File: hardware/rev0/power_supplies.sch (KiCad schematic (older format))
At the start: 35 parts, among them IC1 ECP5-BGA256, U3 MIC5219-3.3YM5, U4 TCR2EE11, U5 MIC5504-2.5YM5

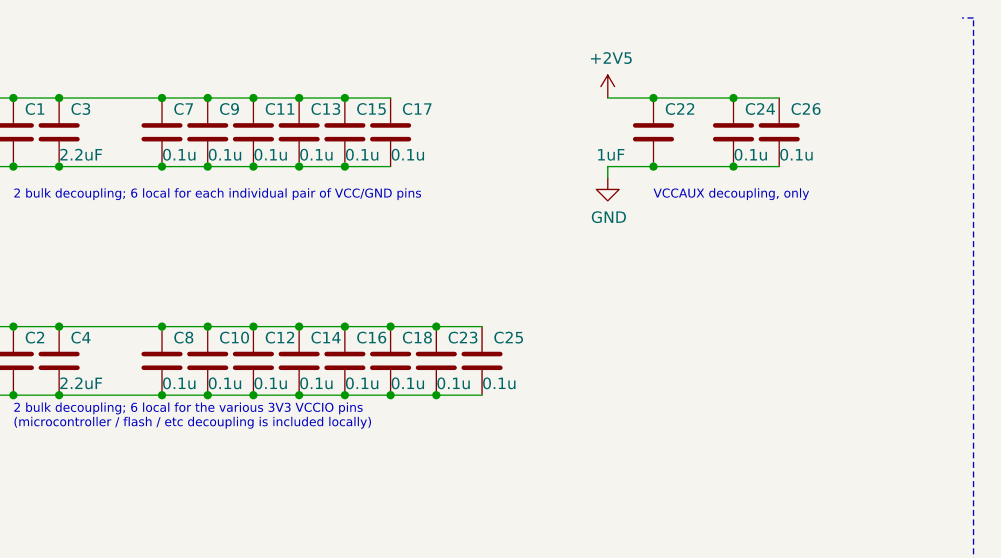
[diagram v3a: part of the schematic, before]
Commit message: Tidy up component values
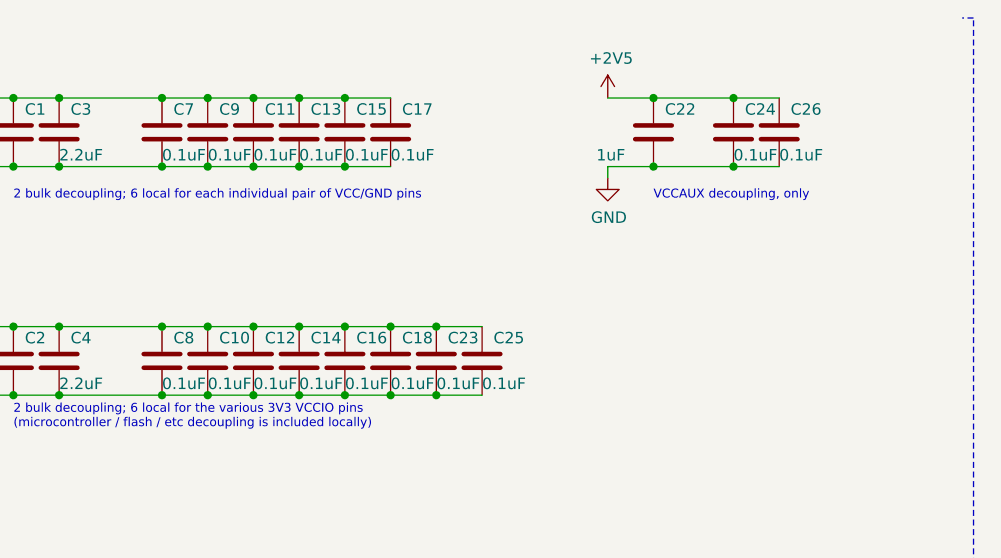
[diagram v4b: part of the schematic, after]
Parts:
- C10, C11, C12, C13, C14, C15, C16, C17, C18, C23, C24, C25, C26, C7, C8, C9: value 0.1u -> 0.1uF
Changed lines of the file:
@@
 P 1700 1000
 F 0 "C7" H 1750 1100 50  0000 L CNN
-F 1 "0.1u" H 1700 900 50  0000 L CNN
+F 1 "0.1uF" H 1700 900 50  0000 L CNN
 F 2 "Capacitor_SMD:C_0402_1005Metric" H 1738 850 50  0001 C CNN
 F 3 "~" H 1700 1000 50  0001 C CNN
@@
 P 1900 1000
 F 0 "C9" H 1950 1100 50  0000 L CNN
-F 1 "0.1u" H 1900 900 50  0000 L CNN
+F 1 "0.1uF" H 1900 900 50  0000 L CNN
 F 2 "Capacitor_SMD:C_0402_1005Metric" H 1938 850 50  0001 C CNN
 F 3 "~" H 1900 1000 50  0001 C CNN
@@
 P 2100 1000
 F 0 "C11" H 2150 1100 50  0000 L CNN
-F 1 "0.1u" H 2100 900 50  0000 L CNN
+F 1 "0.1uF" H 2100 900 50  0000 L CNN
 F 2 "Capacitor_SMD:C_0402_1005Metric" H 2138 850 50  0001 C CNN
 F 3 "~" H 2100 1000 50  0001 C CNN
@@
 P 2300 1000
 F 0 "C13" H 2350 1100 50  0000 L CNN
-F 1 "0.1u" H 2300 900 50  0000 L CNN
+F 1 "0.1uF" H 2300 900 50  0000 L CNN
 F 2 "Capacitor_SMD:C_0402_1005Metric" H 2338 850 50  0001 C CNN
 F 3 "~" H 2300 1000 50  0001 C CNN
@@
 P 2500 1000
 F 0 "C15" H 2550 1100 50  0000 L CNN
-F 1 "0.1u" H 2500 900 50  0000 L CNN
+F 1 "0.1uF" H 2500 900 50  0000 L CNN
 F 2 "Capacitor_SMD:C_0402_1005Metric" H 2538 850 50  0001 C CNN
 F 3 "~" H 2500 1000 50  0001 C CNN
@@
 P 2700 1000
 F 0 "C17" H 2750 1100 50  0000 L CNN
-F 1 "0.1u" H 2700 900 50  0000 L CNN
+F 1 "0.1uF" H 2700 900 50  0000 L CNN
 F 2 "Capacitor_SMD:C_0402_1005Metric" H 2738 850 50  0001 C CNN
 F 3 "~" H 2700 1000 50  0001 C CNN
@@
 P 2500 2000
 F 0 "C16" H 2550 2100 50  0000 L CNN
-F 1 "0.1u" H 2500 1900 50  0000 L CNN
+F 1 "0.1uF" H 2500 1900 50  0000 L CNN
 F 2 "Capacitor_SMD:C_0402_1005Metric" H 2538 1850 50  0001 C CNN
 F 3 "~" H 2500 2000 50  0001 C CNN
@@
 P 2300 2000
 F 0 "C14" H 2350 2100 50  0000 L CNN
-F 1 "0.1u" H 2300 1900 50  0000 L CNN
+F 1 "0.1uF" H 2300 1900 50  0000 L CNN
 F 2 "Capacitor_SMD:C_0402_1005Metric" H 2338 1850 50  0001 C CNN
 F 3 "~" H 2300 2000 50  0001 C CNN
@@
 P 2100 2000
 F 0 "C12" H 2150 2100 50  0000 L CNN
-F 1 "0.1u" H 2100 1900 50  0000 L CNN
+F 1 "0.1uF" H 2100 1900 50  0000 L CNN
 F 2 "Capacitor_SMD:C_0402_1005Metric" H 2138 1850 50  0001 C CNN
 F 3 "~" H 2100 2000 50  0001 C CNN
@@
 P 1900 2000
 F 0 "C10" H 1950 2100 50  0000 L CNN
-F 1 "0.1u" H 1900 1900 50  0000 L CNN
+F 1 "0.1uF" H 1900 1900 50  0000 L CNN
 F 2 "Capacitor_SMD:C_0402_1005Metric" H 1938 1850 50  0001 C CNN
 F 3 "~" H 1900 2000 50  0001 C CNN
@@
 P 1700 2000
 F 0 "C8" H 1750 2100 50  0000 L CNN
-F 1 "0.1u" H 1700 1900 50  0000 L CNN
+F 1 "0.1uF" H 1700 1900 50  0000 L CNN
 F 2 "Capacitor_SMD:C_0402_1005Metric" H 1738 1850 50  0001 C CNN
 F 3 "~" H 1700 2000 50  0001 C CNN
@@
 P 4200 1000
 F 0 "C24" H 4250 1100 50  0000 L CNN
-F 1 "0.1u" H 4200 900 50  0000 L CNN
+F 1 "0.1uF" H 4200 900 50  0000 L CNN
 F 2 "Capacitor_SMD:C_0402_1005Metric" H 4238 850 50  0001 C CNN
 F 3 "~" H 4200 1000 50  0001 C CNN
@@
 P 4400 1000
 F 0 "C26" H 4450 1100 50  0000 L CNN
-F 1 "0.1u" H 4400 900 50  0000 L CNN
+F 1 "0.1uF" H 4400 900 50  0000 L CNN
 F 2 "Capacitor_SMD:C_0402_1005Metric" H 4438 850 50  0001 C CNN
 F 3 "~" H 4400 1000 50  0001 C CNN
@@
 P 3100 2000
 F 0 "C25" H 3150 2100 50  0000 L CNN
-F 1 "0.1u" H 3100 1900 50  0000 L CNN
+F 1 "0.1uF" H 3100 1900 50  0000 L CNN
 F 2 "Capacitor_SMD:C_0402_1005Metric" H 3138 1850 50  0001 C CNN
 F 3 "~" H 3100 2000 50  0001 C CNN
@@
 P 2900 2000
 F 0 "C23" H 2950 2100 50  0000 L CNN
-F 1 "0.1u" H 2900 1900 50  0000 L CNN
+F 1 "0.1uF" H 2900 1900 50  0000 L CNN
 F 2 "Capacitor_SMD:C_0402_1005Metric" H 2938 1850 50  0001 C CNN
 F 3 "~" H 2900 2000 50  0001 C CNN
@@
 P 2700 2000
 F 0 "C18" H 2750 2100 50  0000 L CNN
-F 1 "0.1u" H 2700 1900 50  0000 L CNN
+F 1 "0.1uF" H 2700 1900 50  0000 L CNN
 F 2 "Capacitor_SMD:C_0402_1005Metric" H 2738 1850 50  0001 C CNN
 F 3 "~" H 2700 2000 50  0001 C CNN

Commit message: Pick part numbers for BOM
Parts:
- C1, C2, C20, C3, C4, C6: Manufacturer_Part_Number (none) -> LMK107B7105KA-T
- C10, C11, C12, C13, C14, C15, C16, C17, C18, C23, C24, C25, C26, C27, C7, C8, C9: Manufacturer_Part_Number (none) -> LMF105B7104KVHF
- C22, C28, C29, C30: Manufacturer_Part_Number (none) -> LMK107B7225KA-T
- C52: Manufacturer_Part_Number (none) -> UMK105BJ471KV-F
- U3: Manufacturer_Part_Number (none) -> MIC5219-3.3YM5-TR
- U4: Manufacturer_Part_Number (none) -> TCR2EE11,LM
- U5: Manufacturer_Part_Number (none) -> MIC5219-2.5YM5-TR
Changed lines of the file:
@@
 F 2 "Capacitor_SMD:C_0603_1608Metric" H 4488 5900 50  0001 C CNN
 F 3 "~" H 4450 6050 50  0001 C CNN
+F 4 "LMK107B7225KA-T" H 4450 6050 50  0001 C CNN "Manufacturer_Part_Number"
 	1    4450 6050
 	0    1    1    0
@@
 F 2 "Capacitor_SMD:C_0603_1608Metric" H 5938 6250 50  0001 C CNN
 F 3 "~" H 5900 6400 50  0001 C CNN
+F 4 "LMK107B7225KA-T" H 5900 6400 50  0001 C CNN "Manufacturer_Part_Number"
 	1    5900 6400
 	1    0    0    -1
@@
 F 2 "Package_TO_SOT_SMD:SOT-23-5" H 5350 5950 50  0001 C CNN
 F 3 "http://ww1.microchip.com/downloads/en/DeviceDoc/MIC550X.pdf" H 5100 6600 50  0001 C CNN
+F 4 "MIC5219-2.5YM5-TR" H 5350 6350 50  0001 C CNN "Manufacturer_Part_Number"
 	1    5350 6350
 	1    0    0    -1
@@
 F 2 "Capacitor_SMD:C_0603_1608Metric" H 1488 3750 50  0001 C CNN
 F 3 "~" H 1450 3900 50  0001 C CNN
+F 4 "LMK107B7105KA-T" H 1450 3900 50  0001 C CNN "Manufacturer_Part_Number"
 	1    1450 3900
 	0    1    1    0
@@
 F 2 "Capacitor_SMD:C_0603_1608Metric" H 2988 4100 50  0001 C CNN
 F 3 "~" H 2950 4250 50  0001 C CNN
+F 4 "LMK107B7105KA-T" H 2950 4250 50  0001 C CNN "Manufacturer_Part_Number"
 	1    2950 4250
 	1    0    0    -1
@@
 F 2 "Capacitor_SMD:C_0402_1005Metric" H 4488 3700 50  0001 C CNN
 F 3 "~" H 4450 3850 50  0001 C CNN
+F 4 "LMF105B7104KVHF" H 4450 3850 50  0001 C CNN "Manufacturer_Part_Number"
 	1    4450 3850
 	0    1    1    0
@@
 F 2 "Capacitor_SMD:C_0603_1608Metric" H 5938 4050 50  0001 C CNN
 F 3 "~" H 5900 4200 50  0001 C CNN
+F 4 "LMK107B7225KA-T" H 5900 4200 50  0001 C CNN "Manufacturer_Part_Number"
 	1    5900 4200
 	1    0    0    -1
@@
 F 2 "Capacitor_SMD:C_0402_1005Metric" H 1738 850 50  0001 C CNN
 F 3 "~" H 1700 1000 50  0001 C CNN
+F 4 "LMF105B7104KVHF" H 1700 1000 50  0001 C CNN "Manufacturer_Part_Number"
 	1    1700 1000
 	1    0    0    -1
@@
 F 2 "Capacitor_SMD:C_0402_1005Metric" H 1938 850 50  0001 C CNN
 F 3 "~" H 1900 1000 50  0001 C CNN
+F 4 "LMF105B7104KVHF" H 1900 1000 50  0001 C CNN "Manufacturer_Part_Number"
 	1    1900 1000
 	1    0    0    -1
@@
 F 2 "Capacitor_SMD:C_0402_1005Metric" H 2138 850 50  0001 C CNN
 F 3 "~" H 2100 1000 50  0001 C CNN
+F 4 "LMF105B7104KVHF" H 2100 1000 50  0001 C CNN "Manufacturer_Part_Number"
 	1    2100 1000
 	1    0    0    -1
@@
 F 2 "Capacitor_SMD:C_0402_1005Metric" H 2338 850 50  0001 C CNN
 F 3 "~" H 2300 1000 50  0001 C CNN
+F 4 "LMF105B7104KVHF" H 2300 1000 50  0001 C CNN "Manufacturer_Part_Number"
 	1    2300 1000
 	1    0    0    -1
@@
 F 2 "Capacitor_SMD:C_0402_1005Metric" H 2538 850 50  0001 C CNN
 F 3 "~" H 2500 1000 50  0001 C CNN
+F 4 "LMF105B7104KVHF" H 2500 1000 50  0001 C CNN "Manufacturer_Part_Number"
 	1    2500 1000
 	1    0    0    -1
@@
 F 2 "Capacitor_SMD:C_0402_1005Metric" H 2738 850 50  0001 C CNN
 F 3 "~" H 2700 1000 50  0001 C CNN
+F 4 "LMF105B7104KVHF" H 2700 1000 50  0001 C CNN "Manufacturer_Part_Number"
 	1    2700 1000
 	1    0    0    -1
@@
 F 2 "Capacitor_SMD:C_0603_1608Metric" H 1088 850 50  0001 C CNN
 F 3 "~" H 1050 1000 50  0001 C CNN
+F 4 "LMK107B7105KA-T" H 1050 1000 50  0001 C CNN "Manufacturer_Part_Number"
 	1    1050 1000
 	1    0    0    -1
@@
 F 2 "Capacitor_SMD:C_0603_1608Metric" H 1288 850 50  0001 C CNN
 F 3 "~" H 1250 1000 50  0001 C CNN
+F 4 "LMK107B7105KA-T" H 1250 1000 50  0001 C CNN "Manufacturer_Part_Number"
 	1    1250 1000
 	1    0    0    -1
@@
 F 2 "Capacitor_SMD:C_0603_1608Metric" H 1288 1850 50  0001 C CNN
 F 3 "~" H 1250 2000 50  0001 C CNN
+F 4 "LMK107B7105KA-T" H 1250 2000 50  0001 C CNN "Manufacturer_Part_Number"
 	1    1250 2000
 	1    0    0    -1
@@
 F 2 "Capacitor_SMD:C_0603_1608Metric" H 1088 1850 50  0001 C CNN
 F 3 "~" H 1050 2000 50  0001 C CNN
+F 4 "LMK107B7105KA-T" H 1050 2000 50  0001 C CNN "Manufacturer_Part_Number"
 	1    1050 2000
 	1    0    0    -1
@@
 F 2 "Capacitor_SMD:C_0402_1005Metric" H 2538 1850 50  0001 C CNN
 F 3 "~" H 2500 2000 50  0001 C CNN
+F 4 "LMF105B7104KVHF" H 2500 2000 50  0001 C CNN "Manufacturer_Part_Number"
 	1    2500 2000
 	1    0    0    -1
@@
 F 2 "Capacitor_SMD:C_0402_1005Metric" H 2338 1850 50  0001 C CNN
 F 3 "~" H 2300 2000 50  0001 C CNN
+F 4 "LMF105B7104KVHF" H 2300 2000 50  0001 C CNN "Manufacturer_Part_Number"
 	1    2300 2000
 	1    0    0    -1
@@
 F 2 "Capacitor_SMD:C_0402_1005Metric" H 2138 1850 50  0001 C CNN
 F 3 "~" H 2100 2000 50  0001 C CNN
+F 4 "LMF105B7104KVHF" H 2100 2000 50  0001 C CNN "Manufacturer_Part_Number"
 	1    2100 2000
 	1    0    0    -1
@@
 F 2 "Capacitor_SMD:C_0402_1005Metric" H 1938 1850 50  0001 C CNN
 F 3 "~" H 1900 2000 50  0001 C CNN
+F 4 "LMF105B7104KVHF" H 1900 2000 50  0001 C CNN "Manufacturer_Part_Number"
 	1    1900 2000
 	1    0    0    -1
@@
 F 2 "Capacitor_SMD:C_0402_1005Metric" H 1738 1850 50  0001 C CNN
 F 3 "~" H 1700 2000 50  0001 C CNN
+F 4 "LMF105B7104KVHF" H 1700 2000 50  0001 C CNN "Manufacturer_Part_Number"
 	1    1700 2000
 	1    0    0    -1
@@
 F 2 "Capacitor_SMD:C_0603_1608Metric" H 3888 850 50  0001 C CNN
 F 3 "~" H 3850 1000 50  0001 C CNN
+F 4 "LMK107B7225KA-T" H 3850 1000 50  0001 C CNN "Manufacturer_Part_Number"
 	1    3850 1000
 	1    0    0    -1
@@
 F 2 "Capacitor_SMD:C_0402_1005Metric" H 4238 850 50  0001 C CNN
 F 3 "~" H 4200 1000 50  0001 C CNN
+F 4 "LMF105B7104KVHF" H 4200 1000 50  0001 C CNN "Manufacturer_Part_Number"
 	1    4200 1000
 	1    0    0    -1
@@
 F 2 "Capacitor_SMD:C_0402_1005Metric" H 4438 850 50  0001 C CNN
 F 3 "~" H 4400 1000 50  0001 C CNN
+F 4 "LMF105B7104KVHF" H 4400 1000 50  0001 C CNN "Manufacturer_Part_Number"
 	1    4400 1000
 	1    0    0    -1
@@
 F 2 "Capacitor_SMD:C_0402_1005Metric" H 2688 4300 50  0001 C CNN
 F 3 "~" H 2650 4450 50  0001 C CNN
+F 4 "UMK105BJ471KV-F" H 2650 4450 50  0001 C CNN "Manufacturer_Part_Number"
 	1    2650 4450
 	1    0    0    -1
@@
 F 2 "Package_TO_SOT_SMD:SOT-23-5" H 2350 4525 50  0001 C CNN
 F 3 "http://ww1.microchip.com/downloads/en/DeviceDoc/MIC5219-500mA-Peak-Output-LDO-Regulator-DS20006021A.pdf" H 2350 4200 50  0001 C CNN
+F 4 "MIC5219-3.3YM5-TR" H 2350 4200 50  0001 C CNN "Manufacturer_Part_Number"
 	1    2350 4200
 	1    0    0    -1
@@
 F 2 "Capacitor_SMD:C_0402_1005Metric" H 3138 1850 50  0001 C CNN
 F 3 "~" H 3100 2000 50  0001 C CNN
+F 4 "LMF105B7104KVHF" H 3100 2000 50  0001 C CNN "Manufacturer_Part_Number"
 	1    3100 2000
 	1    0    0    -1
@@
 F 2 "Capacitor_SMD:C_0402_1005Metric" H 2938 1850 50  0001 C CNN
 F 3 "~" H 2900 2000 50  0001 C CNN
+F 4 "LMF105B7104KVHF" H 2900 2000 50  0001 C CNN "Manufacturer_Part_Number"
 	1    2900 2000
 	1    0    0    -1
@@
 F 2 "Capacitor_SMD:C_0402_1005Metric" H 2738 1850 50  0001 C CNN
 F 3 "~" H 2700 2000 50  0001 C CNN
+F 4 "LMF105B7104KVHF" H 2700 2000 50  0001 C CNN "Manufacturer_Part_Number"
 	1    2700 2000
 	1    0    0    -1
@@
 F 2 "Package_TO_SOT_SMD:SOT-553" H 5350 3750 50  0001 C CNN
 F 3 "https://toshiba.semicon-storage.com/info/docget.jsp?did=13794&prodName=TCR2EF45" H 5100 4400 50  0001 C CNN
+F 4 "TCR2EE11,LM" H 5350 4150 50  0001 C CNN "Manufacturer_Part_Number"
 	1    5350 4150
 	1    0    0    -1

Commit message: Fix TCR2EE11 MPN
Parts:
- U4: Manufacturer_Part_Number TCR2EE11,LM -> TCR2EE11,LM(CT
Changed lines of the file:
@@
 F 2 "Package_TO_SOT_SMD:SOT-553" H 5350 3750 50  0001 C CNN
 F 3 "https://toshiba.semicon-storage.com/info/docget.jsp?did=13794&prodName=TCR2EF45" H 5100 4400 50  0001 C CNN
-F 4 "TCR2EE11,LM" H 5350 4150 50  0001 C CNN "Manufacturer_Part_Number"
+F 4 "TCR2EE11,LM(CT" H 5350 4150 50  0001 C CNN "Manufacturer_Part_Number"
 	1    5350 4150
 	1    0    0    -1
